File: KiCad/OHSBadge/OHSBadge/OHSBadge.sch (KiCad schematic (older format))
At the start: 119 parts, among them J4 ZIF-40-0.5, P1 PCB, P2 ISP, P3 FTDI, P4 C3SB, P5 JST_3V7, P6 V_IN, P7 UUSB_B, Q1 DMG2301U-7, Q2 2N7002KW, Q3 BSS84W, Q4 2N7002KW, Q5 2N7002KW, Q6 2N7002KW, Q7 BSS84W, SW1 UP, SW2 SEL, SW3 DOWN, SW4 RST, SW5 MODE, SW6 SW_ON, U1 MCP9700AT-E/TT, U2 ATMEGA328-AU-ND, U3 MCP1700T-33, U4 TXS0108, U5 DS1307, U5/7 I/O, U6 MCP1702T-50, X1 8MHz, X2 32.768kHz

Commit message: BADGEr_v4 OHSBadge added break out pads, and other changes.
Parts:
- AD0, AD1, AD2, AD3, PD11, PD12, PD13, PD2, PD4, PD5, PD6, PD7, PD8, PD9, V1, V2: footprint I/O -> Breakout
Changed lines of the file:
@@
-EESchema Schematic File Version 2  date 13-Jun-13 6:47:58 PM
+EESchema Schematic File Version 2
 LIBS:OHSBadge_sym
 LIBS:power
 LIBS:OHSBadge-cache
-EELAYER 27 0
+EELAYER 24 0
 EELAYER END
 $Descr A4 11693 8268
@@
 F 0 "PD13" H 6600 1350 40  0000 L CNN
 F 1 "I/O" H 6550 1295 30  0001 C CNN
-F 2 "I/O" H 6550 1350 60  0001 C CNN
+F 2 "Breakout" H 6550 1350 60  0001 C CNN
 F 3 "~" H 6550 1350 60  0000 C CNN
 	1    6550 1350
@@
 F 0 "PD12" H 6600 1450 40  0000 L CNN
 F 1 "I/O" H 6550 1395 30  0001 C CNN
-F 2 "I/O" H 6550 1450 60  0001 C CNN
+F 2 "Breakout" H 6550 1450 60  0001 C CNN
 F 3 "~" H 6550 1450 60  0000 C CNN
 	1    6550 1450
@@
 F 0 "PD11" H 6600 1550 40  0000 L CNN
 F 1 "I/O" H 6550 1495 30  0001 C CNN
-F 2 "I/O" H 6550 1550 60  0001 C CNN
+F 2 "Breakout" H 6550 1550 60  0001 C CNN
 F 3 "~" H 6550 1550 60  0000 C CNN
 	1    6550 1550
@@
 F 0 "PD9" H 6600 1750 40  0000 L CNN
 F 1 "I/O" H 6550 1695 30  0001 C CNN
-F 2 "I/O" H 6550 1750 60  0001 C CNN
+F 2 "Breakout" H 6550 1750 60  0001 C CNN
 F 3 "~" H 6550 1750 60  0000 C CNN
 	1    6550 1750
@@
 F 0 "PD8" H 6600 1850 40  0000 L CNN
 F 1 "I/O" H 6550 1795 30  0001 C CNN
-F 2 "I/O" H 6550 1850 60  0001 C CNN
+F 2 "Breakout" H 6550 1850 60  0001 C CNN
 F 3 "~" H 6550 1850 60  0000 C CNN
 	1    6550 1850
@@
 F 0 "PD7" H 6600 2050 40  0000 L CNN
 F 1 "I/O" H 6550 1995 30  0001 C CNN
-F 2 "I/O" H 6550 2050 60  0001 C CNN
+F 2 "Breakout" H 6550 2050 60  0001 C CNN
 F 3 "~" H 6550 2050 60  0000 C CNN
 	1    6550 2050
@@
 F 0 "PD6" H 6600 2150 40  0000 L CNN
 F 1 "I/O" H 6550 2095 30  0001 C CNN
-F 2 "I/O" H 6550 2150 60  0001 C CNN
+F 2 "Breakout" H 6550 2150 60  0001 C CNN
 F 3 "~" H 6550 2150 60  0000 C CNN
 	1    6550 2150
@@
 F 0 "PD5" H 6600 2250 40  0000 L CNN
 F 1 "I/O" H 6550 2195 30  0001 C CNN
-F 2 "I/O" H 6550 2250 60  0001 C CNN
+F 2 "Breakout" H 6550 2250 60  0001 C CNN
 F 3 "~" H 6550 2250 60  0000 C CNN
 	1    6550 2250
@@
 F 0 "PD4" H 6600 2350 40  0000 L CNN
 F 1 "I/O" H 6550 2295 30  0001 C CNN
-F 2 "I/O" H 6550 2350 60  0001 C CNN
+F 2 "Breakout" H 6550 2350 60  0001 C CNN
 F 3 "~" H 6550 2350 60  0000 C CNN
 	1    6550 2350
@@
 F 0 "PD2" H 6600 2550 40  0000 L CNN
 F 1 "I/O" H 6550 2495 30  0001 C CNN
-F 2 "I/O" H 6550 2550 60  0001 C CNN
+F 2 "Breakout" H 6550 2550 60  0001 C CNN
 F 3 "~" H 6550 2550 60  0000 C CNN
 	1    6550 2550
@@
 F 0 "AD3" H 3650 2550 40  0000 L CNN
 F 1 "I/O" H 3600 2495 30  0001 C CNN
-F 2 "I/O" H 3600 2550 60  0001 C CNN
+F 2 "Breakout" H 3600 2550 60  0001 C CNN
 F 3 "~" H 3600 2550 60  0000 C CNN
 	1    3600 2550
@@
 F 0 "AD2" H 3650 2450 40  0000 L CNN
 F 1 "I/O" H 3600 2395 30  0001 C CNN
-F 2 "I/O" H 3600 2450 60  0001 C CNN
+F 2 "Breakout" H 3600 2450 60  0001 C CNN
 F 3 "~" H 3600 2450 60  0000 C CNN
 	1    3600 2450
@@
 F 0 "AD1" H 3650 2350 40  0000 L CNN
 F 1 "I/O" H 3600 2295 30  0001 C CNN
-F 2 "I/O" H 3600 2350 60  0001 C CNN
+F 2 "Breakout" H 3600 2350 60  0001 C CNN
 F 3 "~" H 3600 2350 60  0000 C CNN
 	1    3600 2350
@@
 F 0 "AD0" H 3650 2250 40  0000 L CNN
 F 1 "I/O" H 3600 2195 30  0001 C CNN
-F 2 "I/O" H 3600 2250 60  0001 C CNN
+F 2 "Breakout" H 3600 2250 60  0001 C CNN
 F 3 "~" H 3600 2250 60  0000 C CNN
 	1    3600 2250
@@
 F 0 "V1" H 3650 2050 40  0000 L CNN
 F 1 "I/O" H 3600 1995 30  0001 C CNN
-F 2 "I/O" H 3600 2050 60  0001 C CNN
+F 2 "Breakout" H 3600 2050 60  0001 C CNN
 F 3 "~" H 3600 2050 60  0000 C CNN
 	1    3600 2050
@@
 F 0 "V2" H 3650 1650 40  0000 L CNN
 F 1 "I/O" H 3600 1595 30  0001 C CNN
-F 2 "I/O" H 3600 1650 60  0001 C CNN
+F 2 "Breakout" H 3600 1650 60  0001 C CNN
 F 3 "~" H 3600 1650 60  0000 C CNN
 	1    3600 1650

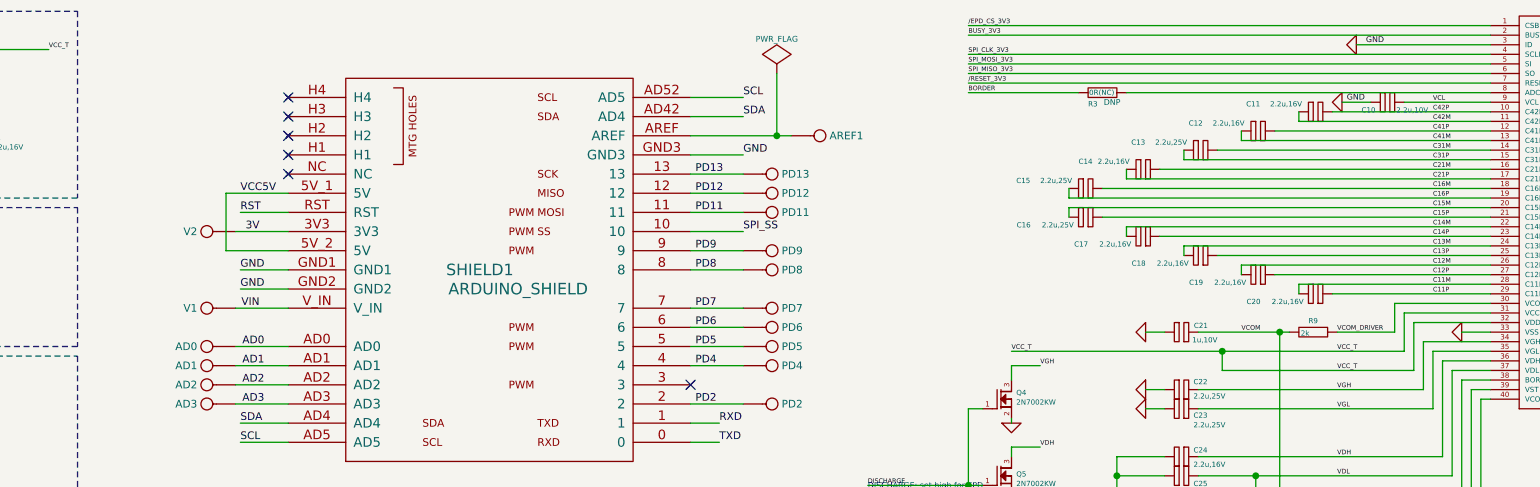
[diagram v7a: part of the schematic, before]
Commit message: OHSBadge : BADGEr_v4. Connected SDA and SCL to I/O H Header. Added project URL.
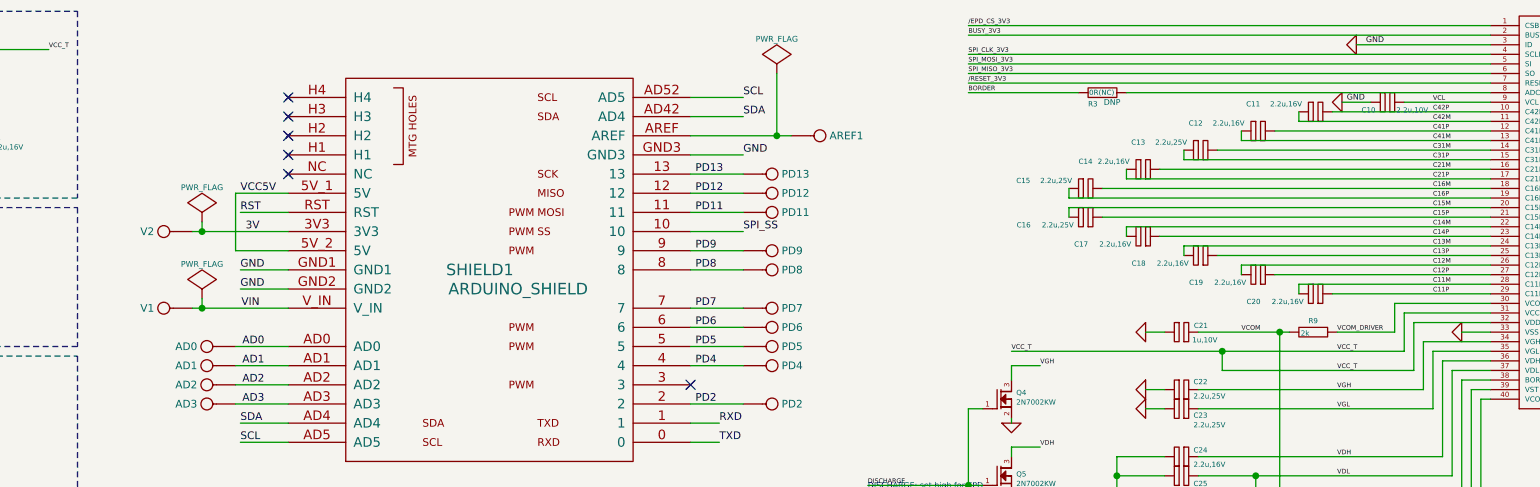
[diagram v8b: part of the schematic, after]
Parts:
- AREF1: footprint I/O -> Breakout
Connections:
- wire segments 375 -> 377
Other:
- moved on the sheet: V1, V2
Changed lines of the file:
@@
-EESchema Schematic File Version 2
+EESchema Schematic File Version 2  date 14-Jun-13 5:11:23 PM
 LIBS:OHSBadge_sym
 LIBS:power
 LIBS:OHSBadge-cache
-EELAYER 24 0
+EELAYER 27 0
 EELAYER END
 $Descr A4 11693 8268
@@
 Sheet 1 1
 Title "BADGEr_v4"
-Date "13 jun 2013"
+Date "14 jun 2013"
 Rev ""
 Comp ""
@@
 	10300 2075 9850 2075
 Wire Wire Line
-	9850 2075 9850 2275
+	9850 2275 9850 2075
 Wire Wire Line
 	8900 2275 8900 2375
@@
 	8700 3975 8700 4075
 Wire Wire Line
-	9850 2275 7800 2275
+	7800 2275 9850 2275
 Wire Wire Line
 	2400 700  2400 1100
@@
 $EndComp
 Wire Wire Line
-	4025 1450 3700 1450
+	4025 1450 3750 1450
 Wire Wire Line
-	3700 1450 3700 1750
+	3750 1450 3750 1750
 Wire Wire Line
-	3700 1750 4025 1750
+	3750 1750 4025 1750
 Wire Wire Line
 	9425 4900 9425 4975
@@
 F 0 "AREF1" H 6850 1150 40  0000 L CNN
 F 1 "I/O" H 6800 1095 30  0001 C CNN
-F 2 "I/O" H 6800 1150 60  0001 C CNN
+F 2 "Breakout" H 6800 1150 60  0001 C CNN
 F 3 "~" H 6800 1150 60  0000 C CNN
 	1    6800 1150
@@
 $EndComp
 Wire Wire Line
-	6650 1150 6125 1150
+	6125 1150 6650 1150
 Text Label 6150 1850 0    40   ~ 0
 PD8
@@
 $EndComp
 Wire Wire Line
-	4025 2050 3750 2050
+	3525 2050 4025 2050
 $Comp
 L I/O V1
 U 1 1 51B9D6B0
-P 3600 2050
-F 0 "V1" H 3650 2050 40  0000 L CNN
-F 1 "I/O" H 3600 1995 30  0001 C CNN
-F 2 "Breakout" H 3600 2050 60  0001 C CNN
-F 3 "~" H 3600 2050 60  0000 C CNN
-	1    3600 2050
+P 3375 2050
+F 0 "V1" H 3425 2050 40  0000 L CNN
+F 1 "I/O" H 3375 1995 30  0001 C CNN
+F 2 "Breakout" H 3375 2050 60  0001 C CNN
+F 3 "~" H 3375 2050 60  0000 C CNN
+	1    3375 2050
 	-1   0    0    1
 $EndComp
@@
 VIN
 Wire Wire Line
-	4025 1650 3750 1650
+	3525 1650 4025 1650
 $Comp
 L I/O V2
 U 1 1 51B9D6C1
-P 3600 1650
-F 0 "V2" H 3650 1650 40  0000 L CNN
-F 1 "I/O" H 3600 1595 30  0001 C CNN
-F 2 "Breakout" H 3600 1650 60  0001 C CNN
-F 3 "~" H 3600 1650 60  0000 C CNN
-	1    3600 1650
+P 3375 1650
+F 0 "V2" H 3425 1650 40  0000 L CNN
+F 1 "I/O" H 3375 1595 30  0001 C CNN
+F 2 "Breakout" H 3375 1650 60  0001 C CNN
+F 3 "~" H 3375 1650 60  0000 C CNN
+	1    3375 1650
 	-1   0    0    1
 $EndComp
 Text Label 3875 1650 2    40   ~ 0
 3V
+$Comp
+L PWR_FLAG #FLG031
+U 1 1 51BAFB74
+P 3575 2000
+F 0 "#FLG031" H 3575 2095 30  0001 C CNN
+F 1 "PWR_FLAG" H 3575 2180 30  0000 C CNN
+F 2 "" H 3575 2000 60  0000 C CNN
+F 3 "" H 3575 2000 60  0000 C CNN
+	1    3575 2000
+	1    0    0    -1
+$EndComp
+$Comp
+L PWR_FLAG #FLG032
+U 1 1 51BAFB81
+P 3575 1600
+F 0 "#FLG032" H 3575 1695 30  0001 C CNN
+F 1 "PWR_FLAG" H 3575 1780 30  0000 C CNN
+F 2 "" H 3575 1600 60  0000 C CNN
+F 3 "" H 3575 1600 60  0000 C CNN
+	1    3575 1600
+	1    0    0    -1
+$EndComp
+Wire Wire Line
+	3575 2000 3575 2050
+Connection ~ 3575 2050
+Wire Wire Line
+	3575 1600 3575 1650
+Connection ~ 3575 1650
 $EndSCHEMATC
